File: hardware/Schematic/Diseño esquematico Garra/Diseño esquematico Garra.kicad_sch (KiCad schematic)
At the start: 14 parts, among them U2 ESP32-WROOM-32

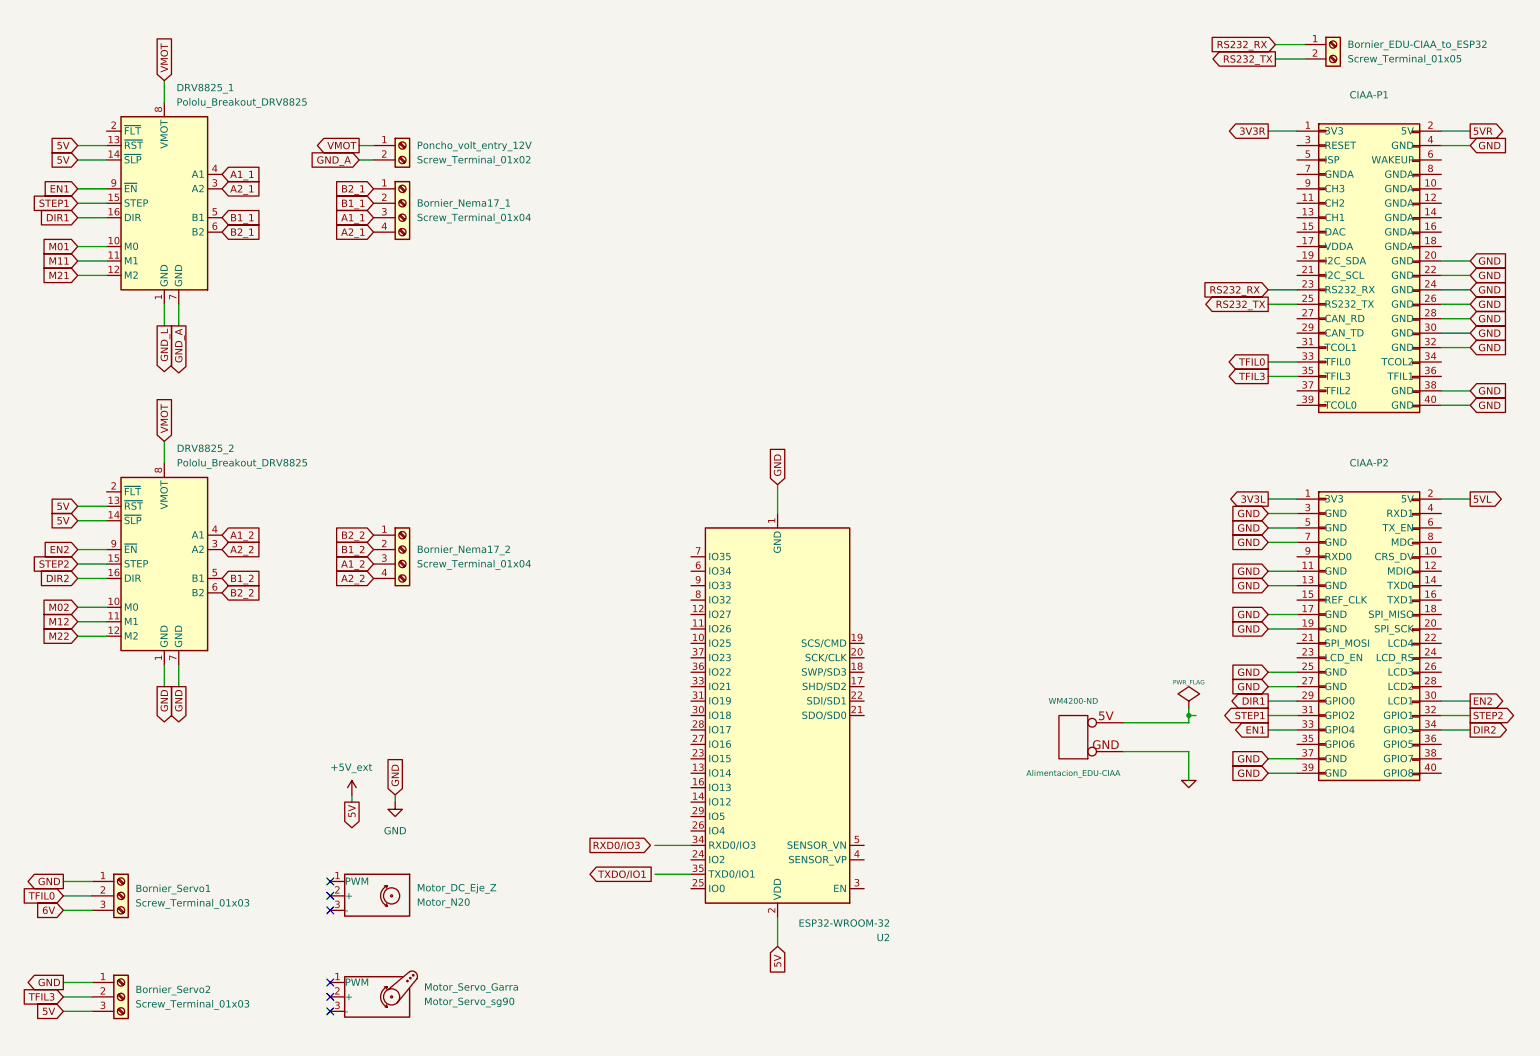
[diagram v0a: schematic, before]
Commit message: schematic update
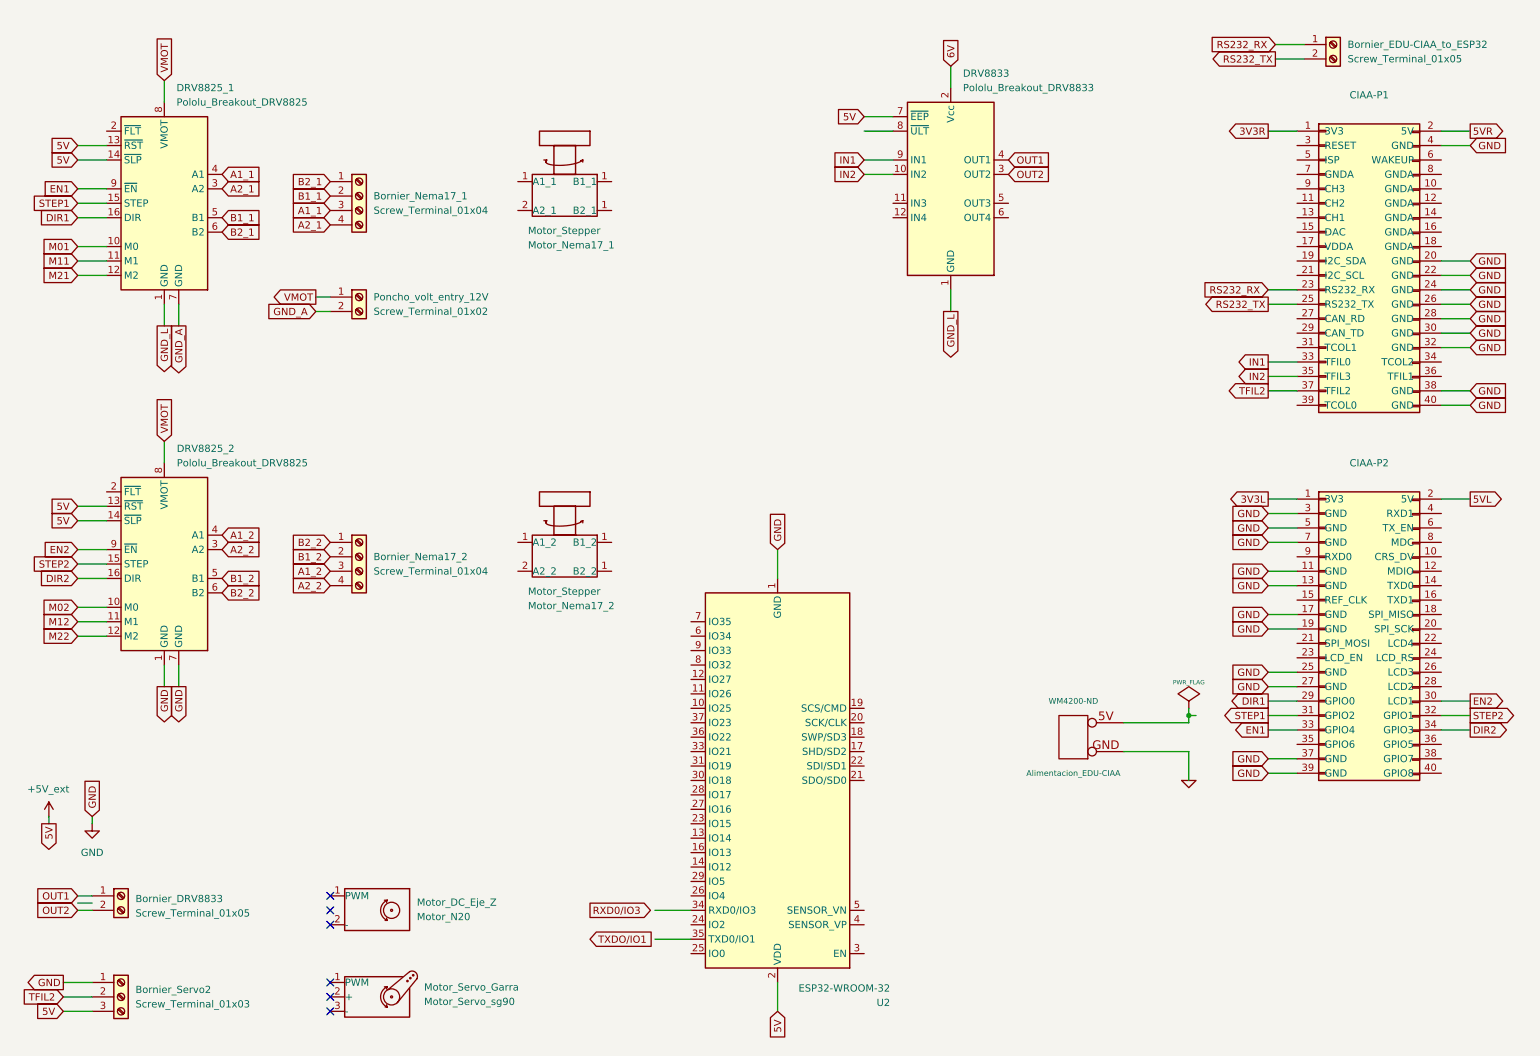
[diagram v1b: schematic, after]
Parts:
- removed Bornier_Servo1: Screw_Terminal_01x03, ProyectoTdL:TerminalBlock_bornier-3_P5.08mm, symbol Connector:Screw_Terminal_01x03
- added Bornier_DRV8833: Screw_Terminal_01x05, ProyectoTdL:TerminalBlock_bornier-2_P5.08mm, symbol Connector:Screw_Terminal_01x02
- added DRV8833: Pololu_Breakout_DRV8833, Module:Pololu_Breakout-16_15.2x20.3mm, symbol Driver_Motor:Pololu_Breakout_DRV8825
- added Motor_Stepper: Motor_Nema17_2, symbol Motor:Motor_Servo
- added Motor_Stepper: Motor_Nema17_1, symbol Motor:Motor_Servo
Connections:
- net +5V_ext: now also DRV8833.7 (~{EEP})
- net 6V: now also DRV8833.2 (Vcc)
- net GND_L: now also DRV8833.1 (GND)
- net TFIL2: now reaches CIAA-P1.37 (TFIL2)
- net TFIL2: now also Bornier_Servo2.2 (Pin_2)
- net TFIL0 renamed IN1
- net IN1: now also DRV8833.9 (IN1)
- net TFIL3 renamed IN2
- net IN2: now also DRV8833.10 (IN2); no longer Bornier_Servo2.2 (Pin_2)
- new net OUT1: Bornier_DRV8833.1 (Pin_1), DRV8833.4 (OUT1)
- new net OUT2: Bornier_DRV8833.2 (Pin_2), DRV8833.3 (OUT2)
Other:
- moved on the sheet: Bornier_Nema17_1, Bornier_Nema17_2, Poncho_volt_entry_12V, U2

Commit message: Added buttons/potentimeter to schematics
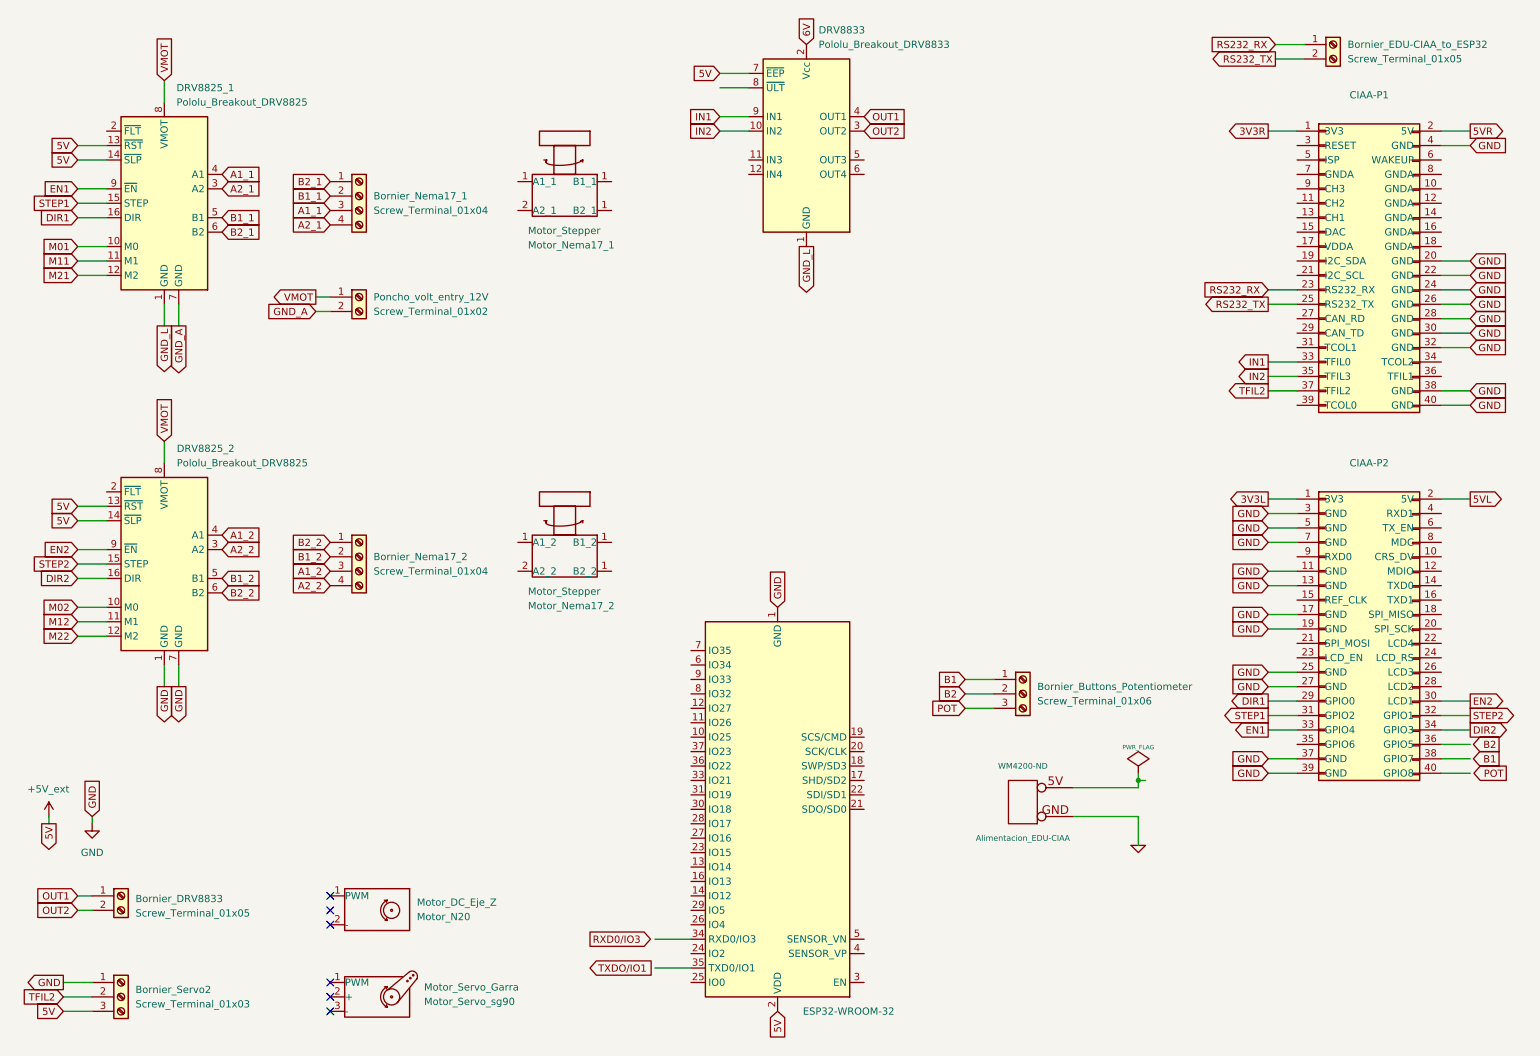
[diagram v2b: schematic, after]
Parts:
- added Bornier_Buttons_Potentiometer: Screw_Terminal_01x06, ProyectoTdL:TerminalBlock_bornier-3_P5.08mm, symbol Connector:Screw_Terminal_01x03
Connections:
- new net B1: Bornier_Buttons_Potentiometer.1 (Pin_1)
- new net B2: Bornier_Buttons_Potentiometer.2 (Pin_2)
- new net POT: Bornier_Buttons_Potentiometer.3 (Pin_3)
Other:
- moved on the sheet: Alimentacion_EDU-CIAA, DRV8833
